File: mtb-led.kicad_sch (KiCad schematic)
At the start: 46 parts, among them J7 AVR-ISP-6, SW1 SW_Push, U1 ATmega328PB-A, U2 78M05, U3 TLC5940PWP, U4 TLC5940PWP, U5 MAX487E, Y1 14.7456 MHz

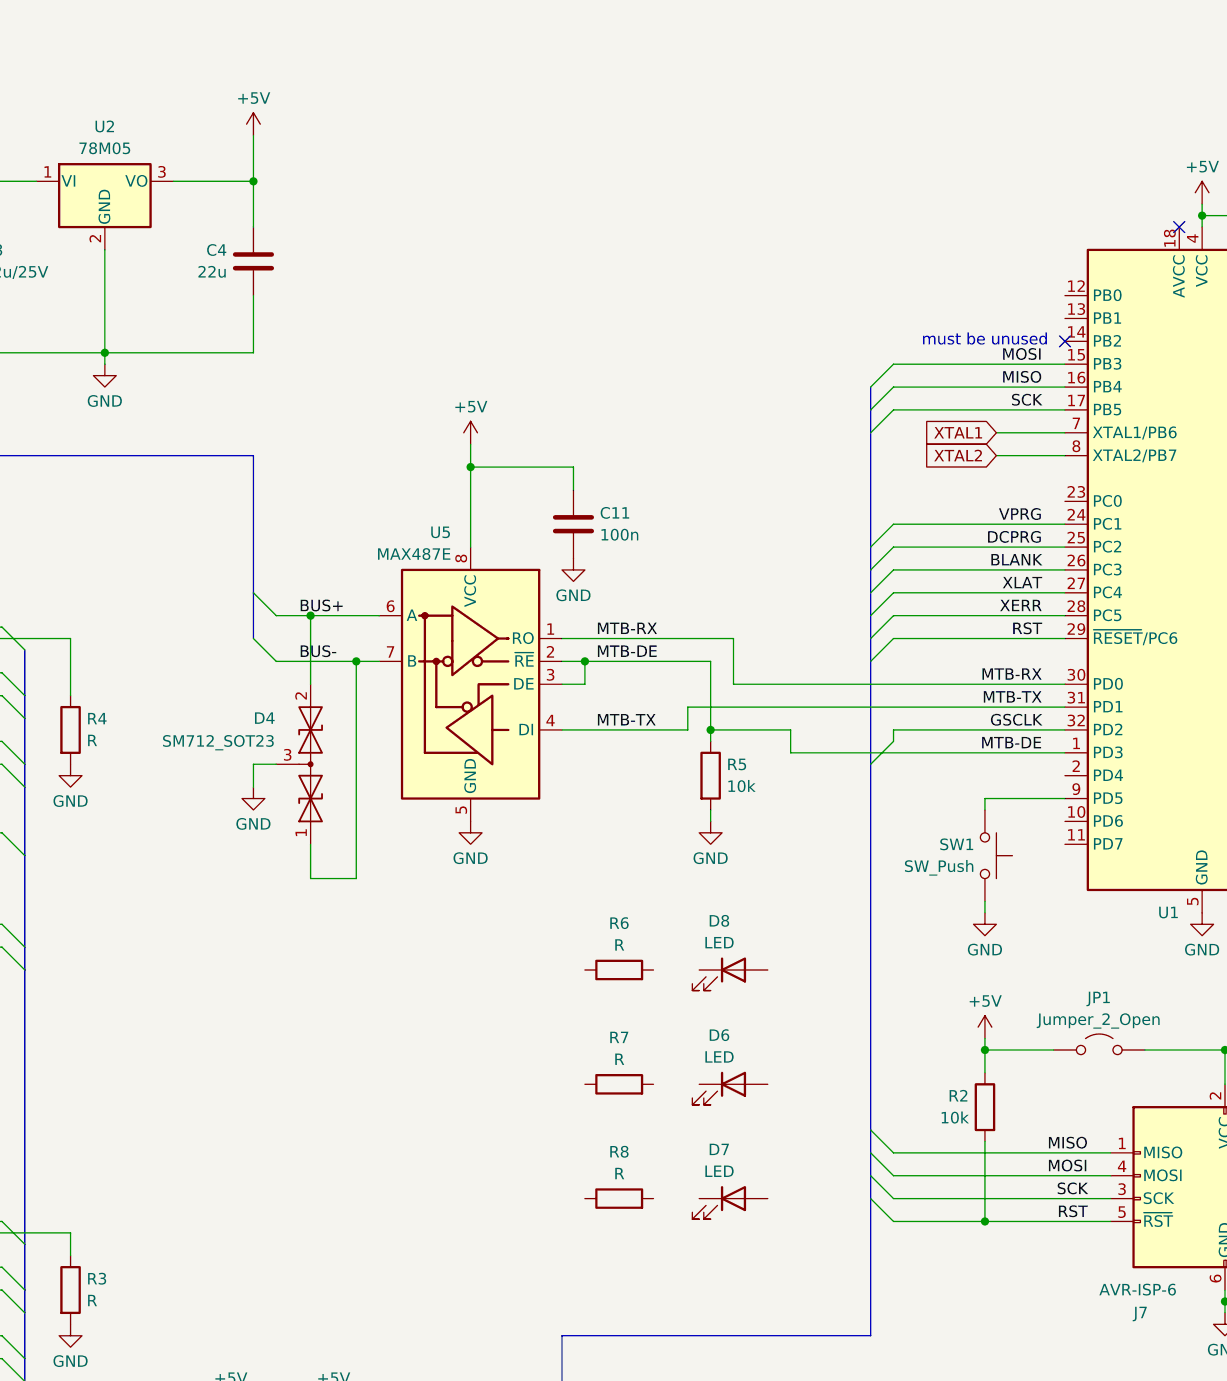
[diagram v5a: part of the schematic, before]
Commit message: Add LEDs.
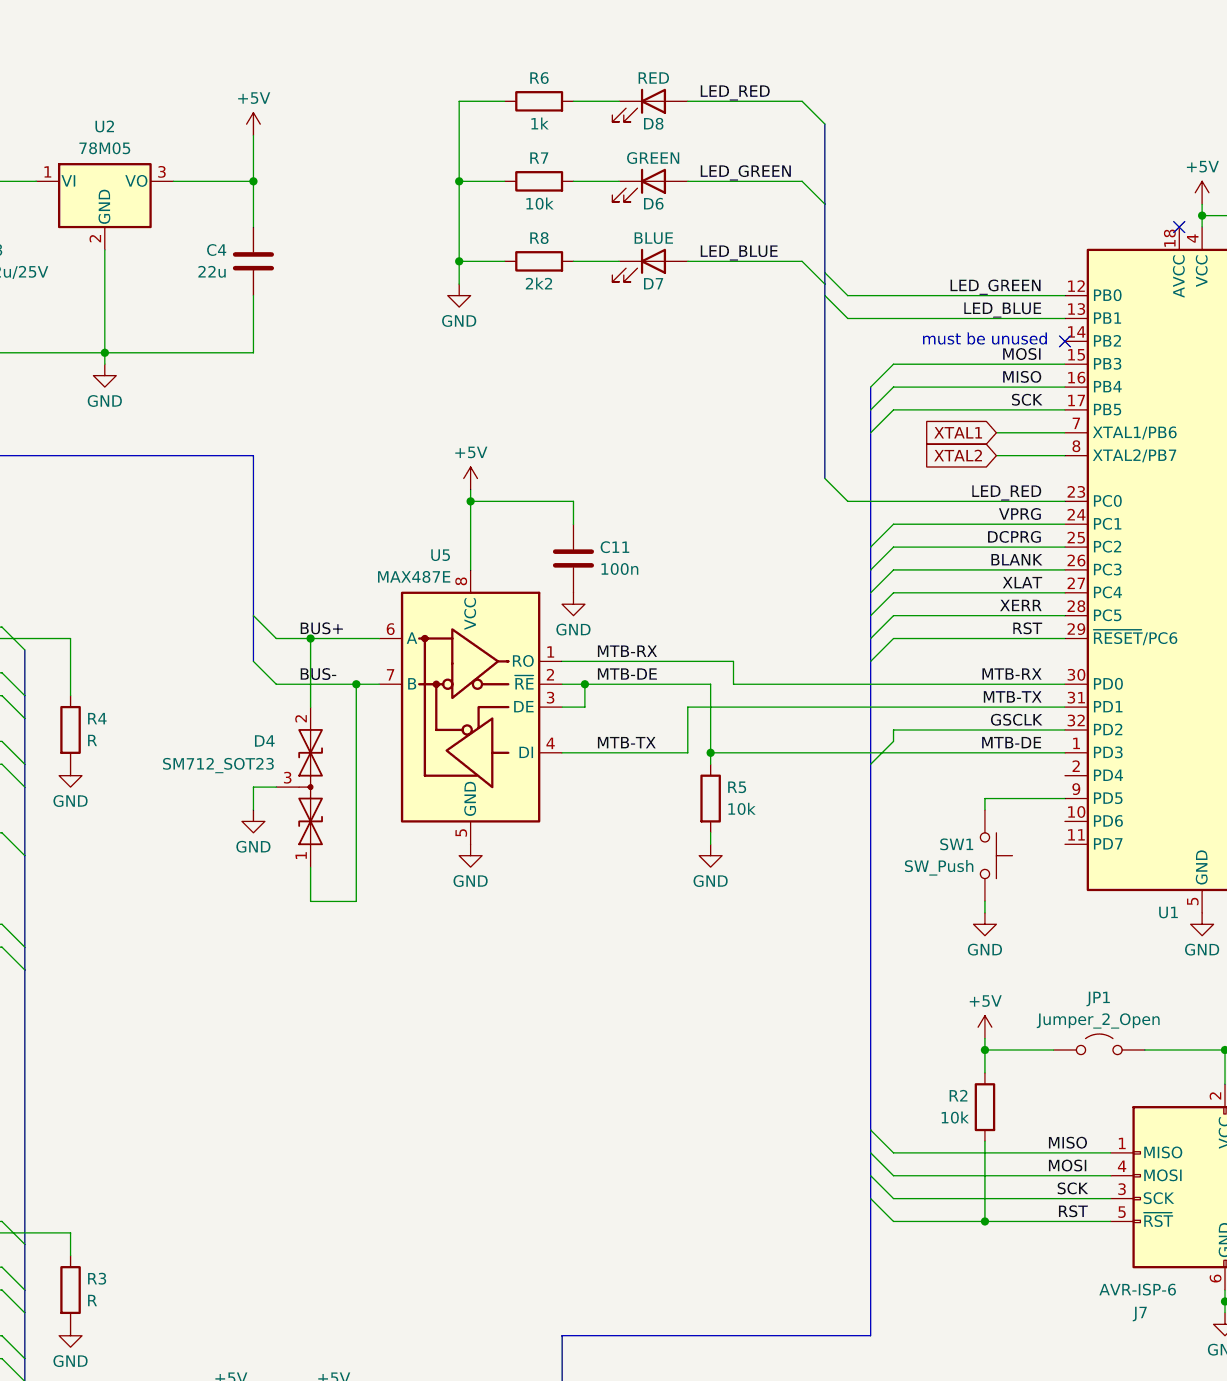
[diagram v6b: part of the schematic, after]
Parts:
- D6: value LED -> GREEN
- D7: value LED -> BLUE
- D8: value LED -> RED
- R6: value R -> 1k
- R7: value R -> 10k
- R8: value R -> 2k2
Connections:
- net GND: now also R6.1, R7.1, R8.1
- net at R7.2: now also D6.1 (K)
- net LED_GREEN: now reaches U1.12 (PB0)
- net LED_GREEN: now also D6.2 (A)
- net LED_BLUE: now reaches U1.13 (PB1)
- net LED_BLUE: now also D7.2 (A)
- net LED_RED: now reaches U1.23 (PC0)
- net LED_RED: now also D8.2 (A)
- net at R8.2: now also D7.1 (K)
- net at D8.1 (K): now also R6.2
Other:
- moved on the sheet: C11, D4, D6, D7, D8, R5, R6, R7, R8, U5

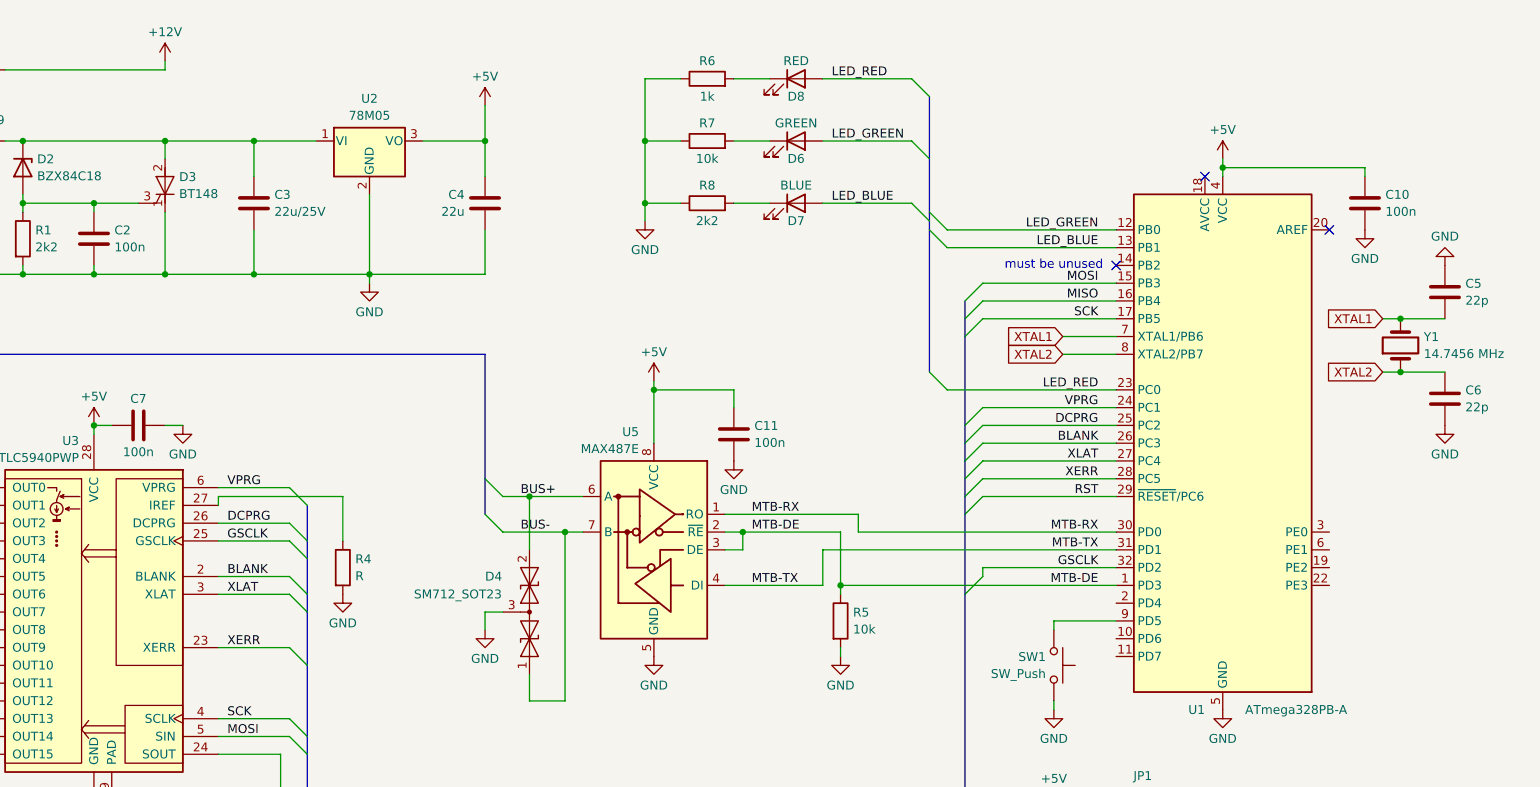
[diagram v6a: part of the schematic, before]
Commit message: Add debug pinheader.
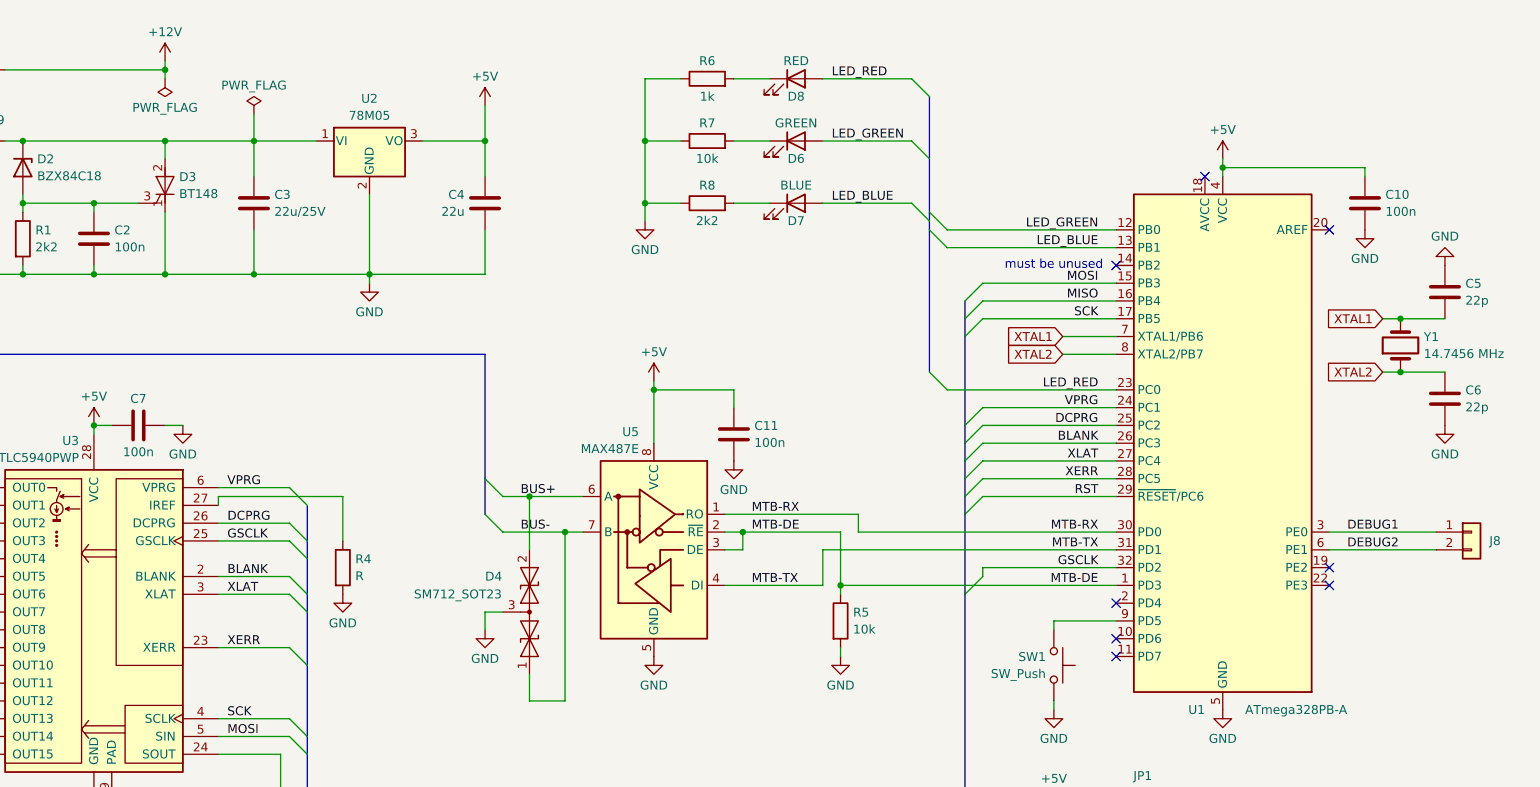
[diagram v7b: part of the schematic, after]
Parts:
- added J8: ~, symbol Connector_Generic:Conn_01x02
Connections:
- net DEBUG1: now reaches U1.3 (PE0)
- net DEBUG1: now also J8.1 (Pin_1)
- net DEBUG2: now reaches U1.6 (PE1)
- net DEBUG2: now also J8.2 (Pin_2)
- no-connect marks 6 -> 11

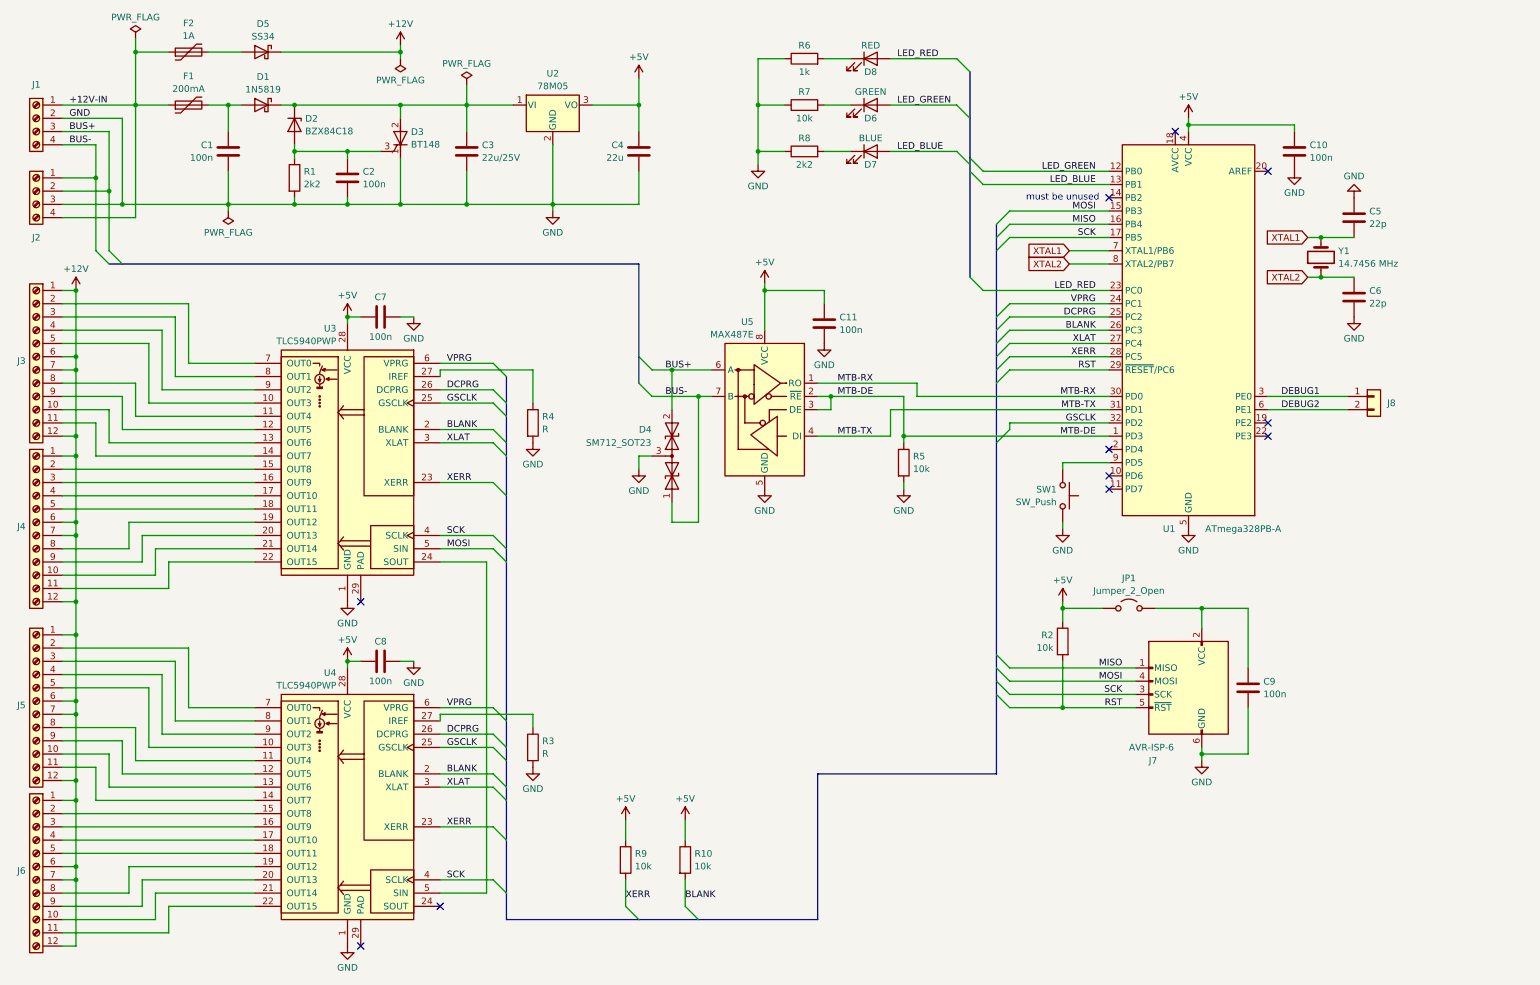
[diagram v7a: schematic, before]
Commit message: Set max LED current (20 ma), add more debug ifaces.
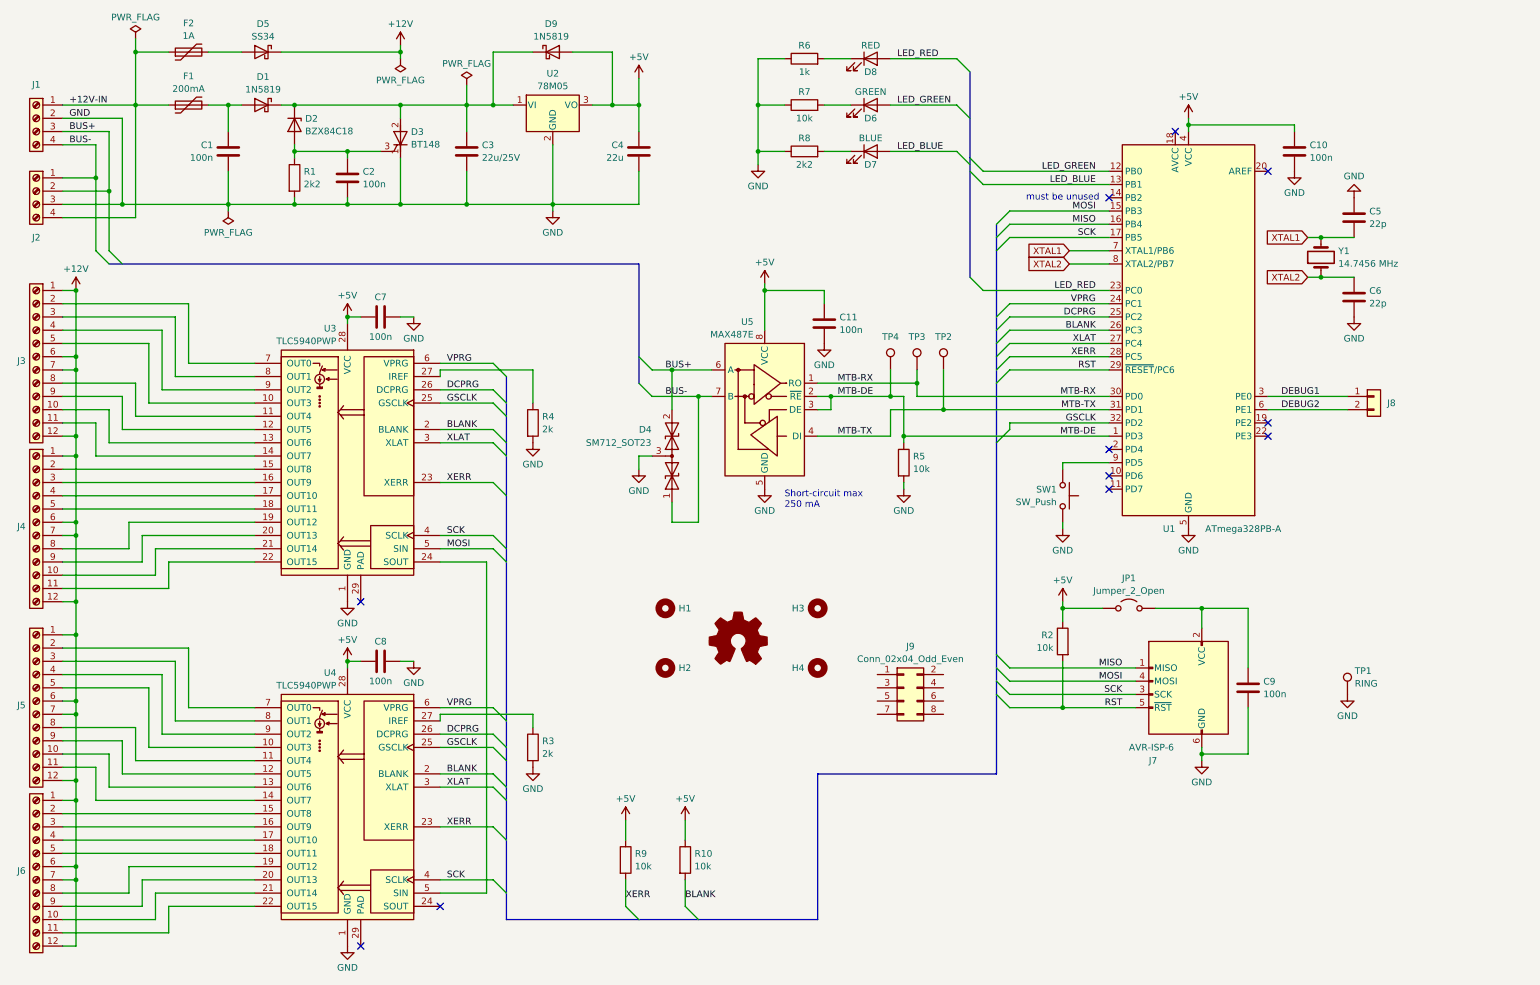
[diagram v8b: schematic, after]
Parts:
- added D9: 1N5819, symbol Device:D_Schottky
- added H1, H2, H3, H4: ~, symbol Mechanical:MountingHole
- added J9: Conn_02x04_Odd_Even, symbol Connector_Generic:Conn_02x04_Odd_Even
- added TP1: RING, symbol Connector:TestPoint
- added TP2, TP3, TP4: ~, symbol Connector:TestPoint
- R3, R4: value R -> 2k
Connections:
- net +5V: now also D9.2 (A)
- net GND: now also TP1.1
- net MTB-DE: now also TP4.1
- net MTB-RX: now also TP3.1
- net MTB-TX: now also TP2.1
- net at C3.1, D1.1 (K), D2.3 (K)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: now also D9.1 (K)
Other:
- note added: "Short-circuit max 250 mA"
